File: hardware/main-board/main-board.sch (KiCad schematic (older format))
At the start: 76 parts, among them J1 USB_B_Micro, J2 DNI, J3 Display Connector, J4 Conn_01x02, SW1 SW_Push, SW2 SW_Push, SW3 SW_Push, SW4 SW_Push, SW5 SW_Detect, U1 TSL2591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

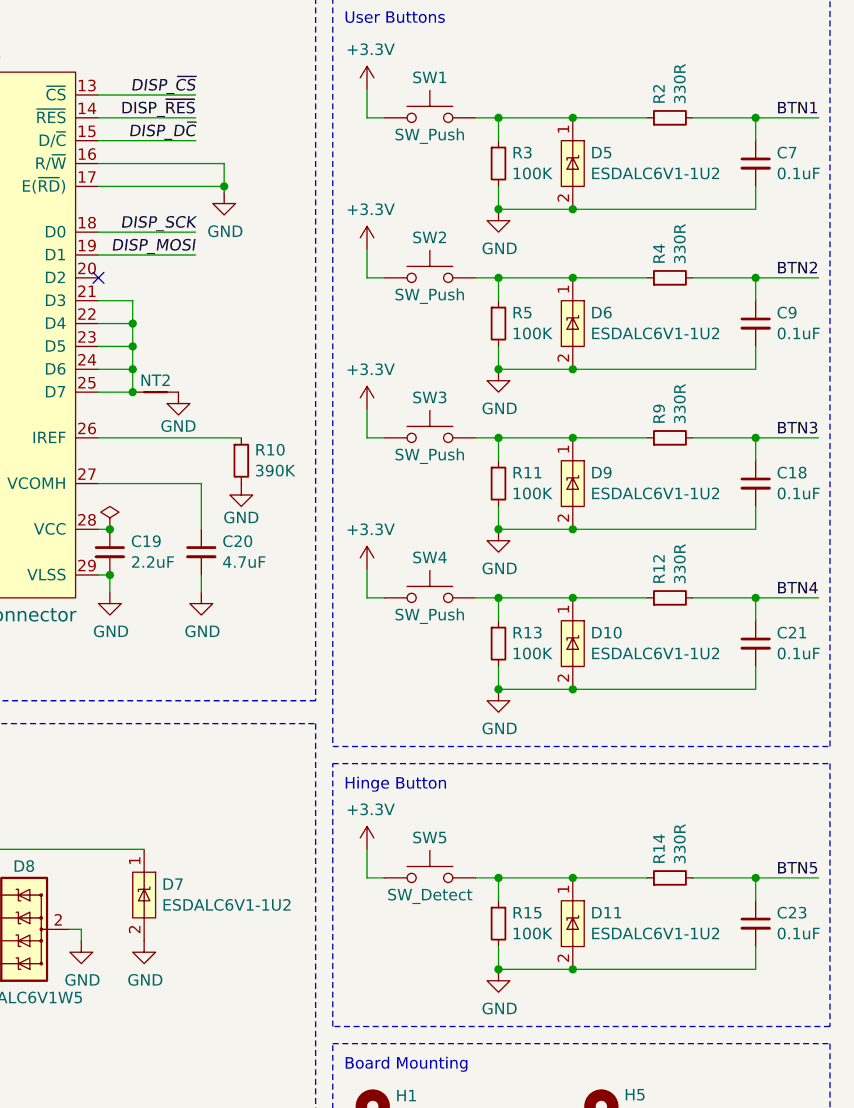
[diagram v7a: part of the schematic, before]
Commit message: Switch single-line TVS diode components
Switch the existing single-line TVS diodes to a slightly larger
component.

Refs #10
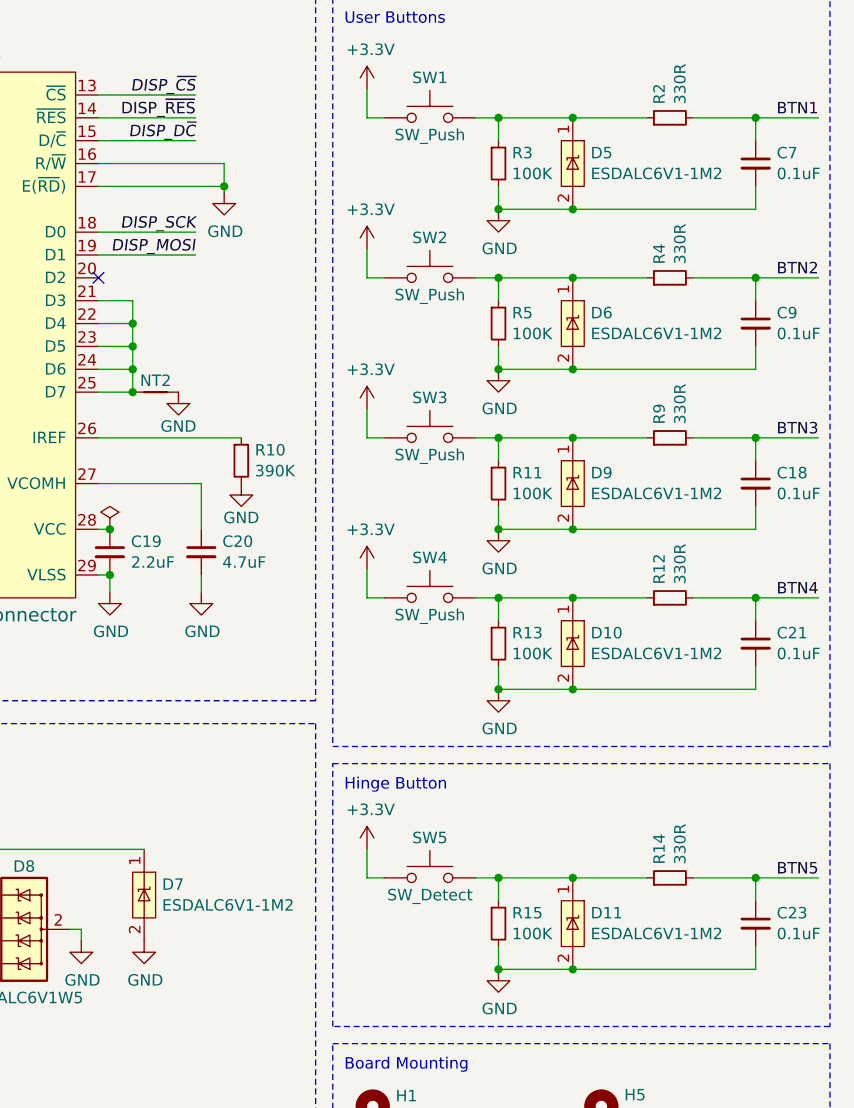
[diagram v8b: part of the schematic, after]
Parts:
- removed D10, D11, D5, D6, D7, D9: ESDALC6V1-1U2, lib_fp:ST0201, symbol Project:ESDALC6V1-1U2
- added D10, D11, D5, D6, D7, D9: ESDALC6V1-1M2, lib_fp:D_SOD-882, symbol Project:ESDALC6V1-1M2
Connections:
- net GND: now also D10.2 (GND), D11.2 (GND), D5.2 (GND), D6.2 (GND), D7.2 (GND), D9.2 (GND)
- net RESET: now also D7.1 (IO1)
- net at R2.1, R3.1, SW1.2: now also D5.1 (IO1)
- net at R4.1, R5.1, SW2.2: now also D6.1 (IO1)
- net at R11.1, R9.1, SW3.2: now also D9.1 (IO1)
- net at R12.1, R13.1, SW4.2: now also D10.1 (IO1)
- net at R14.1, R15.1, SW5.2: now also D11.1 (IO1)
